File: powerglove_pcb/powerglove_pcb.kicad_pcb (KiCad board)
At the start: 2 copper layers, 19 parts, among them J1 Conn_01x02, J2 Conn_01x05, J3 Conn_01x07, J4 Conn_01x02, J5 Conn_01x05, J6 Conn_01x03, J7 Conn_01x03, Q1 BSS123, Q2 BSS123, U1 DRV2605

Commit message: some prelimiary layout placement b4 nap
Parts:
- moved J2 47.3 mm to (113.3, 76.7), turned to 90 degrees
- moved J3 46.6 mm to (88.9, 77.2), turned to 90 degrees
- moved J1 38.6 mm to (118.9, 72.1), turned to 180 degrees
- moved J5 34.6 mm to (71.9, 77.2), turned to 90 degrees
- moved C2 32.2 mm to (87.6, 73.7)
- moved J4 27.2 mm to (104.6, 70.6), turned to 270 degrees
- moved U1 25.2 mm to (94.0, 71.1)
- moved R1 25.0 mm to (87.6, 69.8)
- moved R3 24.9 mm to (89.2, 63.6), turned to 90 degrees
- moved C1 18.5 mm to (92.5, 68.1)
- moved Q1 18.4 mm to (87.9, 58.9), turned to 90 degrees
- moved R5 17.7 mm to (86.6, 63.6), turned to 90 degrees
- moved C3 17.5 mm to (99.1, 71.1), turned to 270 degrees
- moved R2 15.1 mm to (87.6, 71.8)
- moved Q2 13.7 mm to (95.5, 58.9), turned to 90 degrees
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
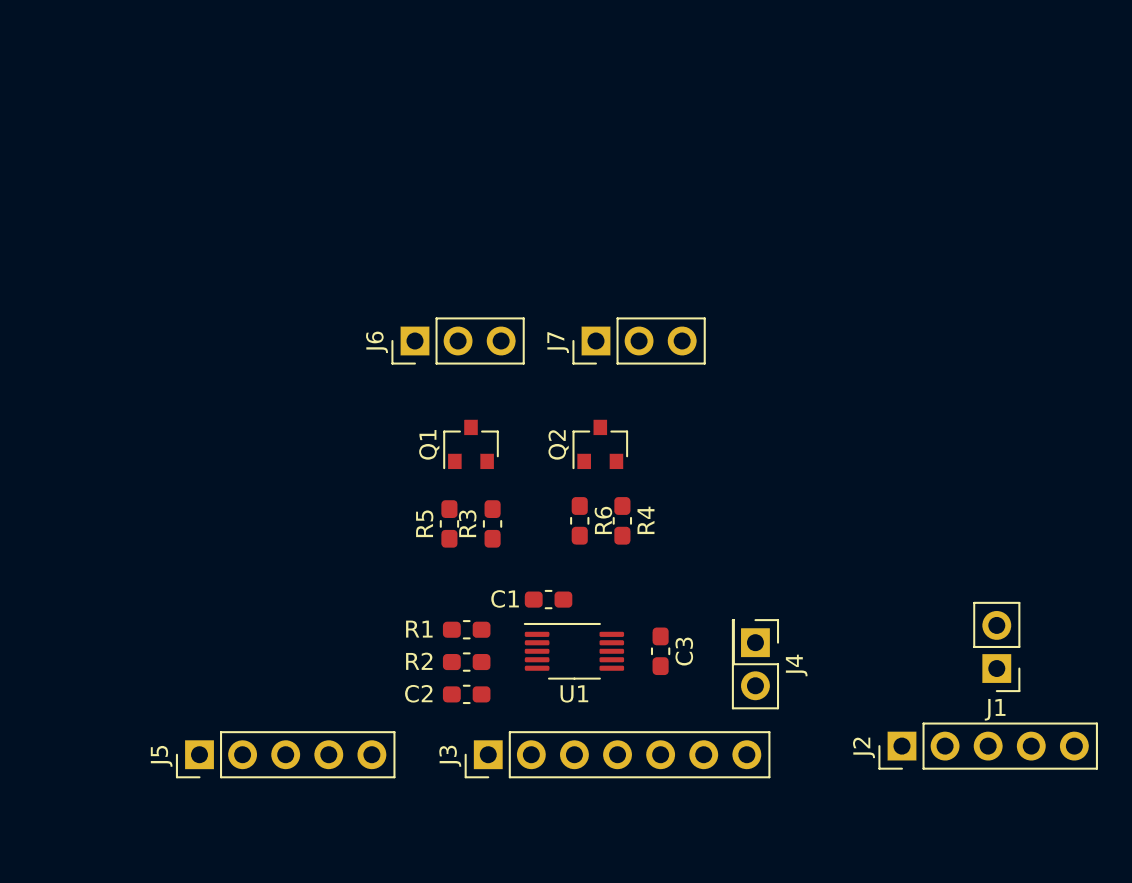
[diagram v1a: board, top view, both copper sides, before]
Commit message: Added ToF sensor header, arrange layout
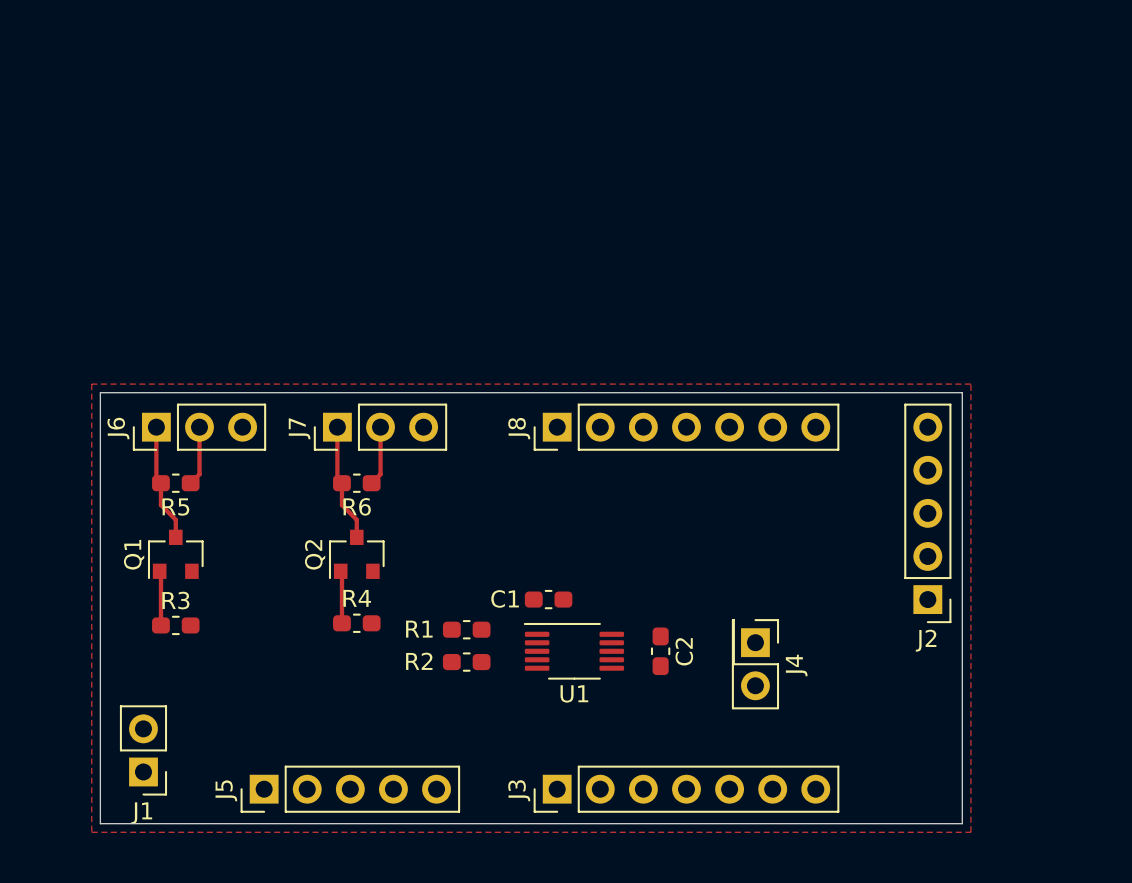
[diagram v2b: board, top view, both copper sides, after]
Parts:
- removed the C2 at (87.6, 73.7)
- added J8: Conn_01x07, Connector_PinHeader_2.54mm:PinHeader_1x07_P2.54mm_Vertical, F.Cu at (93.0, 57.9)
- moved J1 50.7 mm to (68.6, 78.2)
- moved R3 19.6 mm to (70.5, 69.6), turned to 0 degrees
- moved Q1 18.6 mm to (70.5, 65.4)
- moved R4 16.8 mm to (81.2, 69.5), turned to 0 degrees
- moved R5 16.3 mm to (70.5, 61.2), turned to 180 degrees
- moved J6 16.1 mm to (69.3, 57.9)
- moved J7 16.1 mm to (80.0, 57.9)
- moved Q2 15.7 mm to (81.2, 65.4)
- moved R6 13.3 mm to (81.2, 61.2), turned to 180 degrees
- moved J2 8.77 mm to (114.8, 68.1), turned to 180 degrees
- moved J3 4.54 mm to (93.0, 79.2)
- moved J5 4.32 mm to (75.7, 79.2)
- renumbered C3 to C2
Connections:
- U1 pad 4: Net-(C2-Pad1) -> /INT
- U1 pad 8: GND -> (no net)
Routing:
- net +5V: track 0.00 -> 7.04 mm
- net Net-(J7-Pad1): track 0.00 -> 6.97 mm
- net Net-(J6-Pad1): track 0.00 -> 6.97 mm
- net /SERVO1: track 0.00 -> 3.22 mm
- net /SERVO2: track 0.00 -> 3.10 mm
- added copper zone on F.Cu, net GND
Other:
- board outline added: 50.8 x 25.4 mm
- rule trace_min: 0.2 -> 0.1524

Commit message: PCB layout complete
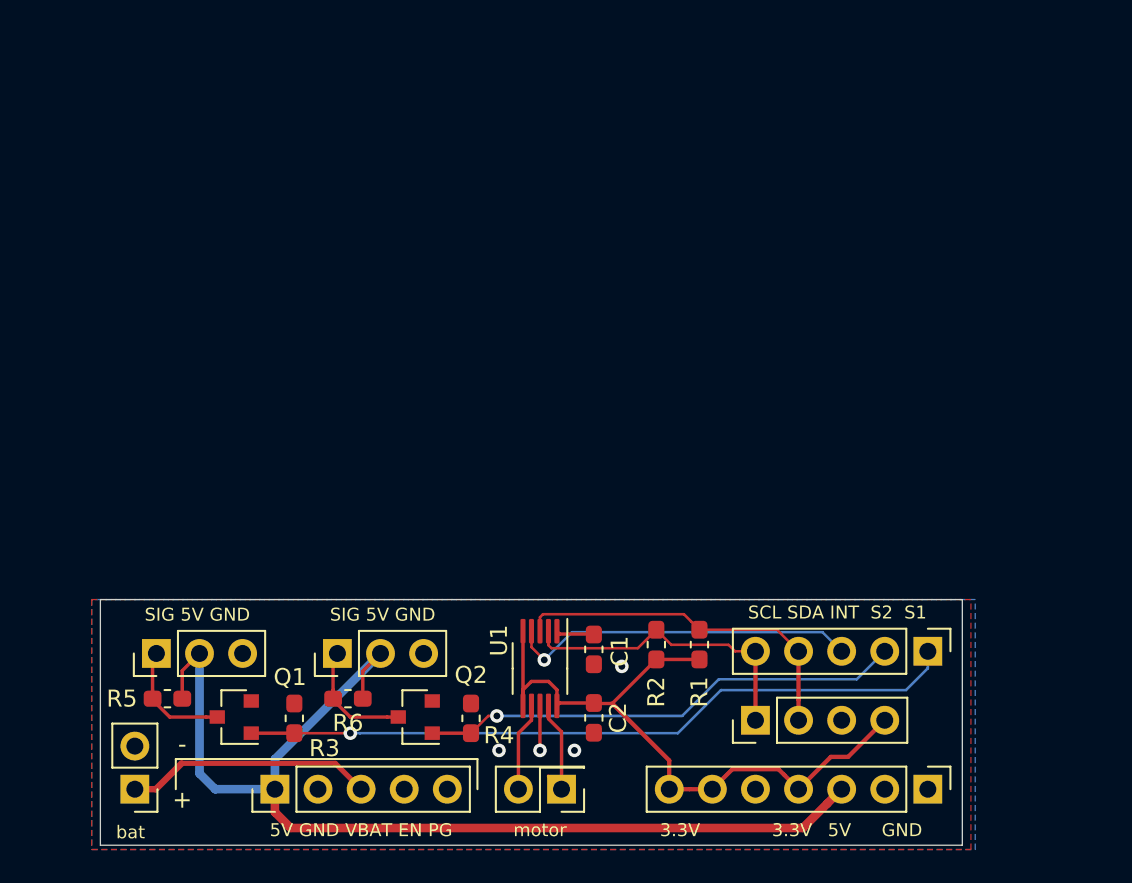
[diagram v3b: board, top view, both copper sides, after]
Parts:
- added G***: LOGO, powerglove_pcb:froge, B.Cu at (85.1, 75.6)
- J8: value Conn_01x07 -> Conn_01x04; footprint Connector_PinHeader_2.54mm:PinHeader_1x07_P2.54mm_Vertical -> Connector_PinHeader_2.54mm:PinHeader_1x04_P2.54mm_Vertical
- moved J3 21.8 mm to (114.8, 79.2), turned to 270 degrees
- moved J8 20.9 mm to (104.6, 75.2)
- moved J4 14.3 mm to (93.2, 79.2), turned to 180 degrees
- moved R1 13.7 mm to (101.3, 70.7), turned to 90 degrees
- moved J6 13.3 mm to (69.3, 71.2)
- moved J7 13.3 mm to (80.0, 71.2)
- moved R6 12.7 mm to (80.6, 73.9)
- moved R5 12.7 mm to (70.0, 73.9)
- moved R2 11.2 mm to (98.8, 70.7), turned to 90 degrees
- moved Q1 10.2 mm to (73.9, 75.0), turned to 180 degrees
- moved Q2 10.2 mm to (84.6, 75.0), turned to 180 degrees
- moved R3 8.88 mm to (77.5, 75.1), turned to 90 degrees
- moved R4 8.76 mm to (87.9, 75.1), turned to 90 degrees
- moved C2 5.56 mm to (95.1, 75.0)
- moved C1 3.97 mm to (95.1, 71.0), turned to 270 degrees
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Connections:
- J2 pad 1: /SERVO2 -> /SERVO1
- J2 pad 2: /SERVO1 -> /SERVO2
- J8 pad 1: Net-(J8-Pad1) -> /SCL
- J8 pad 2: Net-(J8-Pad2) -> /SDA
- J8 pad 3: /SCL -> GND
- J8 pad 4: /SDA -> +3V3
- U1 pad 8: (no net) -> GND
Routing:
- net +5V: track 7.04 -> 64.8 mm
- net +3V3: track 0.00 -> 40.0 mm
- net /SERVO1: track 3.22 -> 42.5 mm, vias 0 -> 1
- net /SERVO2: track 3.10 -> 28.7 mm, vias 0 -> 1
- net /SDA: track 0.00 -> 21.1 mm
- net /INT: track 0.00 -> 20.7 mm, vias 0 -> 1
- net /SCL: track 0.00 -> 18.1 mm
- net /VBAT: track 0.00 -> 14.6 mm
- net Net-(J4-Pad1): track 0.00 -> 6.32 mm
- net Net-(J4-Pad2): track 0.00 -> 5.23 mm
- net GND: track 0.00 -> 2.63 mm, vias 0 -> 4
- net Net-(C1-Pad1): track 0.00 -> 1.86 mm
- net Net-(J7-Pad1): track 6.97 -> 7.74 mm
- net Net-(J6-Pad1): track 6.97 -> 7.70 mm
- added copper zone on B.Cu, net GND
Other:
- board size 50.8 x 25.4 mm -> 50.8 x 14.5 mm
- board text added: "- +"
- board text added: "3.3V"
- board text added: "5V"
- board text added: "5V GND VBAT EN PG"
- board text added: "GND"
- board text added: "SCL SDA INT S2 S1"
- board text added: "SIG 5V GND"
- board text added: "bat"
- board text added: "motor"
- board text added: "powerglove daugherboard 2020"

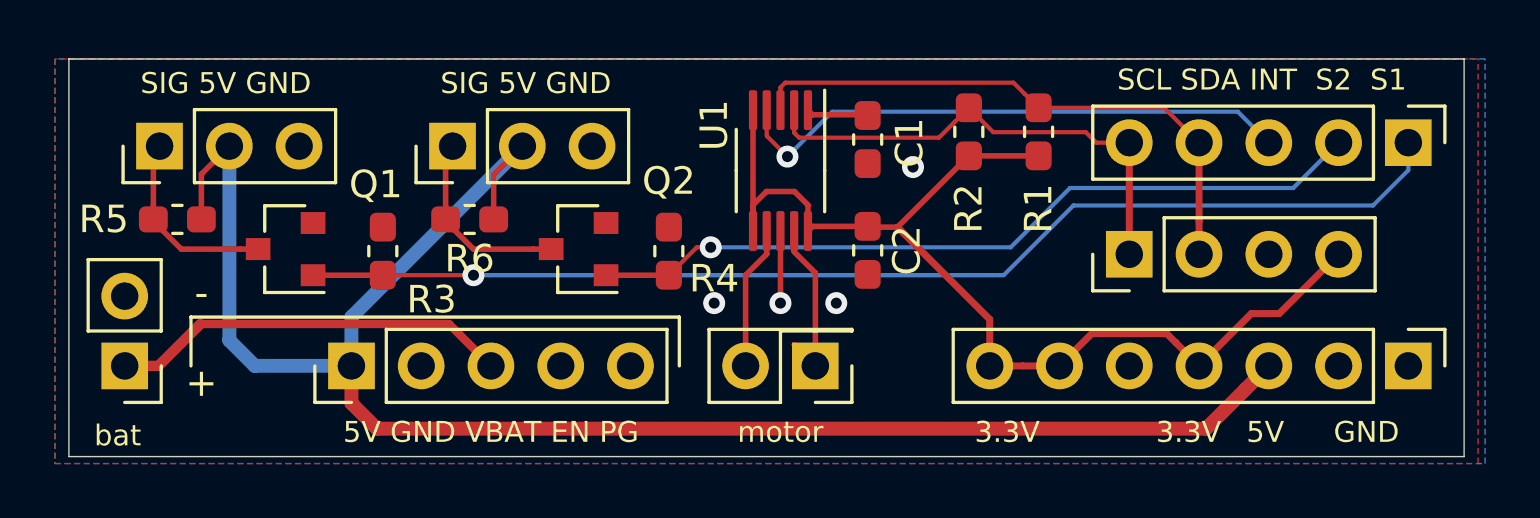
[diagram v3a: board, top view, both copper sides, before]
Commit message: update PCB layout for simple battery monitoring, clean up silk
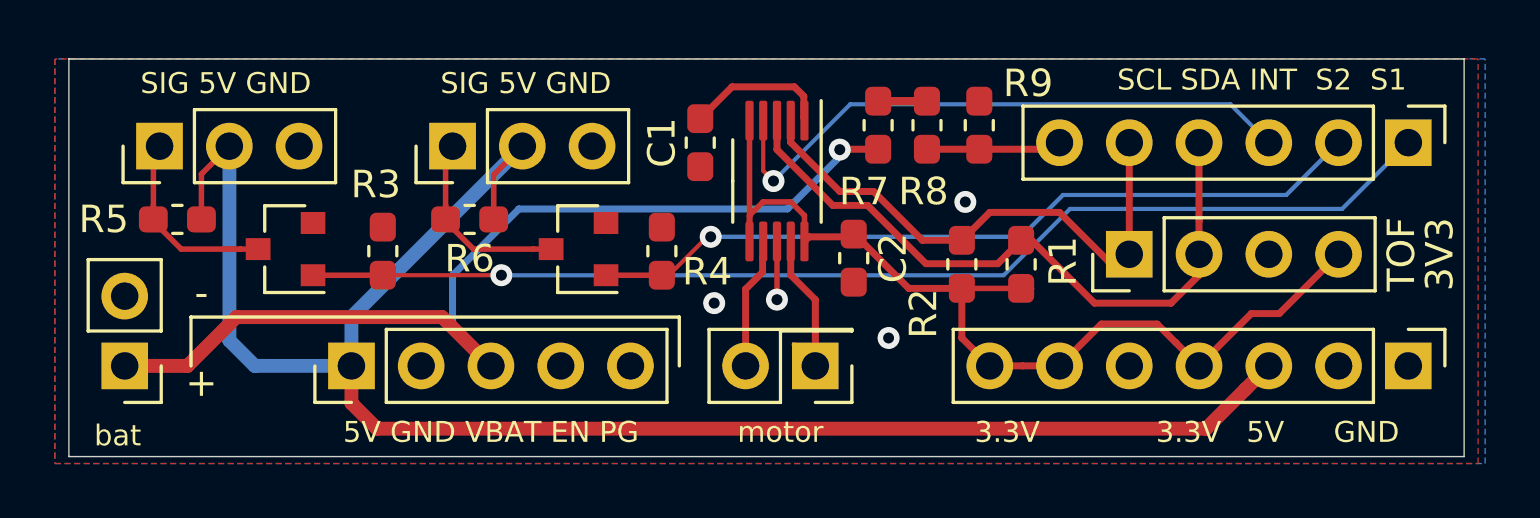
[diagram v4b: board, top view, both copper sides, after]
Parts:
- removed G***: LOGO, powerglove_pcb:froge
- added R7: 10k, Resistor_SMD:R_0603_1608Metric_Pad1.05x0.95mm_HandSolder, F.Cu at (95.5, 70.5)
- added R8: 10k, Resistor_SMD:R_0603_1608Metric_Pad1.05x0.95mm_HandSolder, F.Cu at (97.3, 70.5)
- added R9: 10k, Resistor_SMD:R_0603_1608Metric_Pad1.05x0.95mm_HandSolder, F.Cu at (99.2, 70.5)
- J2: value Conn_01x05 -> Conn_01x06; footprint Connector_PinHeader_2.54mm:PinHeader_1x05_P2.54mm_Vertical -> Connector_PinHeader_2.54mm:PinHeader_1x06_P2.54mm_Vertical
- moved C1 6.10 mm to (89.0, 71.1)
- moved R1 4.87 mm to (100.7, 75.6)
- moved R2 4.83 mm to (98.6, 75.6)
- moved C2 0.58 mm to (94.6, 75.3)
- moved U1 0.40 mm to (91.8, 72.5)
- moved R4 0.25 mm to (87.6, 75.1)
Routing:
- net /VBAT: track 14.6 -> 36.2 mm, vias 0 -> 1
- net /monitor: track 0.00 -> 5.31 mm
- net /SDA: track 21.1 -> 24.7 mm
- net Net-(C1-Pad1): track 1.86 -> 5.29 mm
- net +3V3: track 40.0 -> 36.8 mm
- net /SCL: track 18.1 -> 20.1 mm
- net Net-(R7-Pad2): track 0.00 -> 1.78 mm
- net /INT: track 20.7 -> 22.1 mm
- net /SERVO1: track 42.5 -> 41.9 mm
- net GND: track 2.63 -> 2.12 mm
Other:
- board text added: "3V3"
- board text added: "TOF"

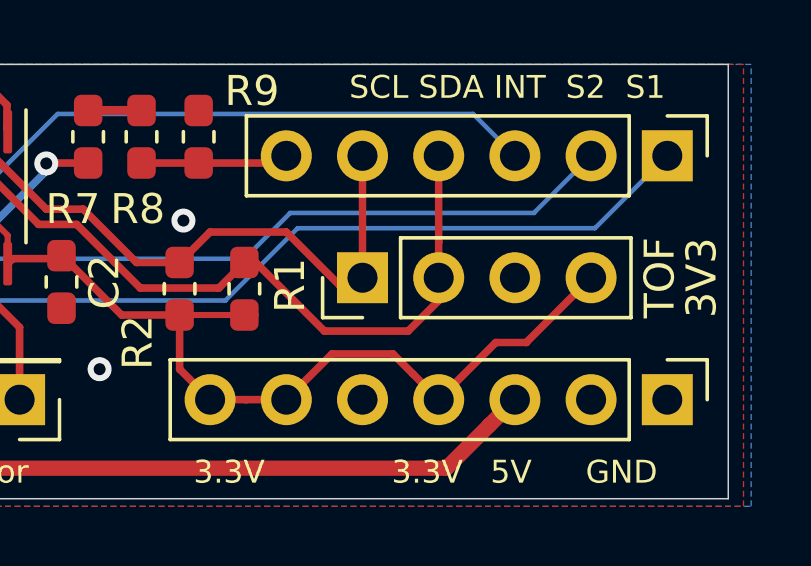
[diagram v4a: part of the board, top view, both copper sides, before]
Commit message: PCB pictures, froge, and supplied driver for ToF sensor (not yet ported)
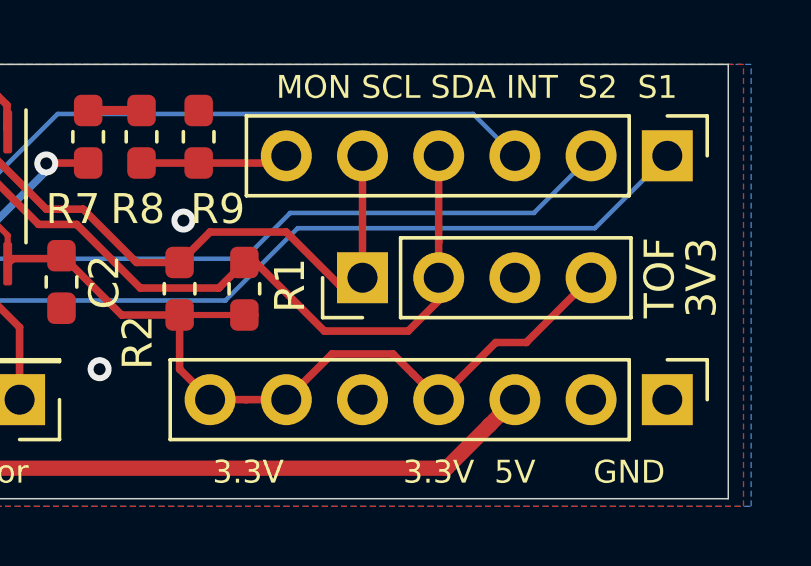
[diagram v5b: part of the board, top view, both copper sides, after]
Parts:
- added G***: LOGO, powerglove_pcb:froge, B.Cu at (95.1, 75.1)
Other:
- board text added: "MON SCL SDA INT S2 S1"
- board text removed: "SCL SDA INT S2 S1"

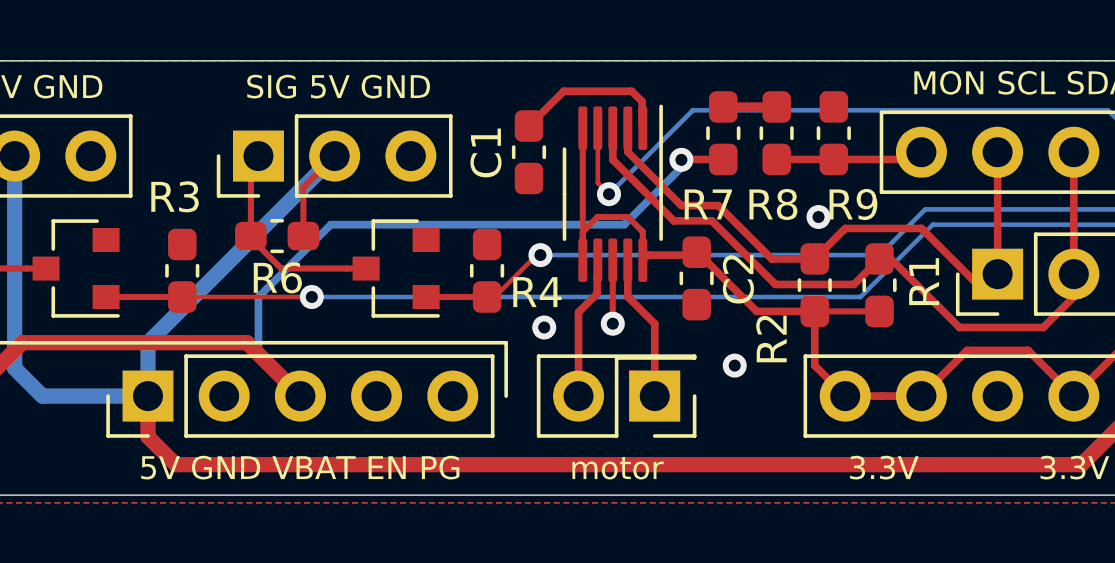
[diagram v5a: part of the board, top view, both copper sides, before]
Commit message: update raytraced pcb images and adjusted PCB back zone
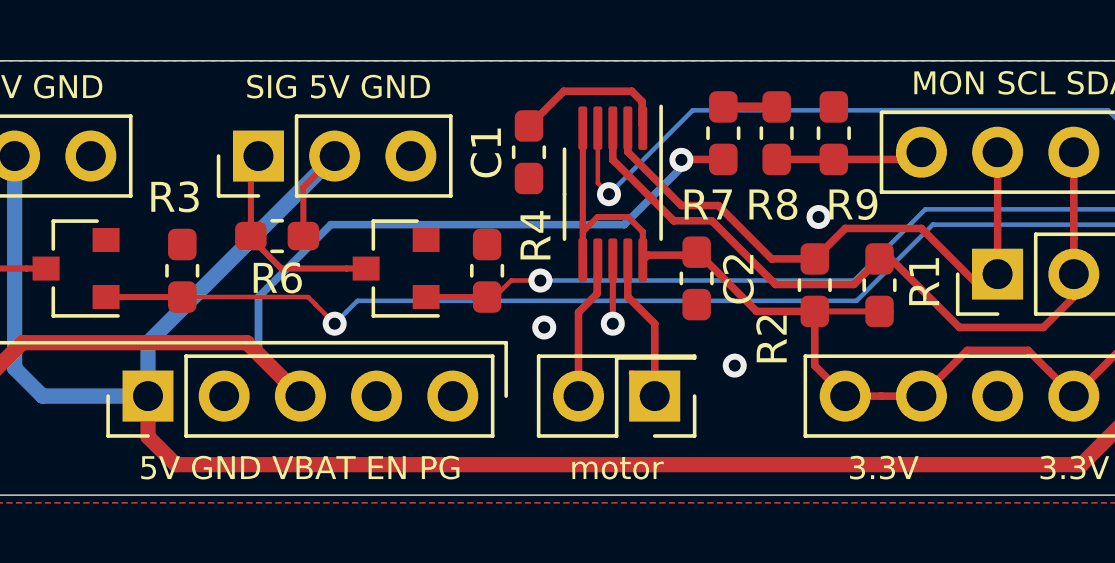
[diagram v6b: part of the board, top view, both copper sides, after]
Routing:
- net /SERVO1: track 41.9 -> 42.6 mm
